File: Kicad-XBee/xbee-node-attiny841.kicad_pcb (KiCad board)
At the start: 2 copper layers, 58.5 x 56.8 mm, 21 parts, among them P1 Program, P2 XBee Adaptor, P3 CONN_5X2, P4 Battery, Q1 S1133, Q2 S9014, Q3 2N7000, U1 ATTINY4313-S, U2 MAX952ESA, U3 TPS77033

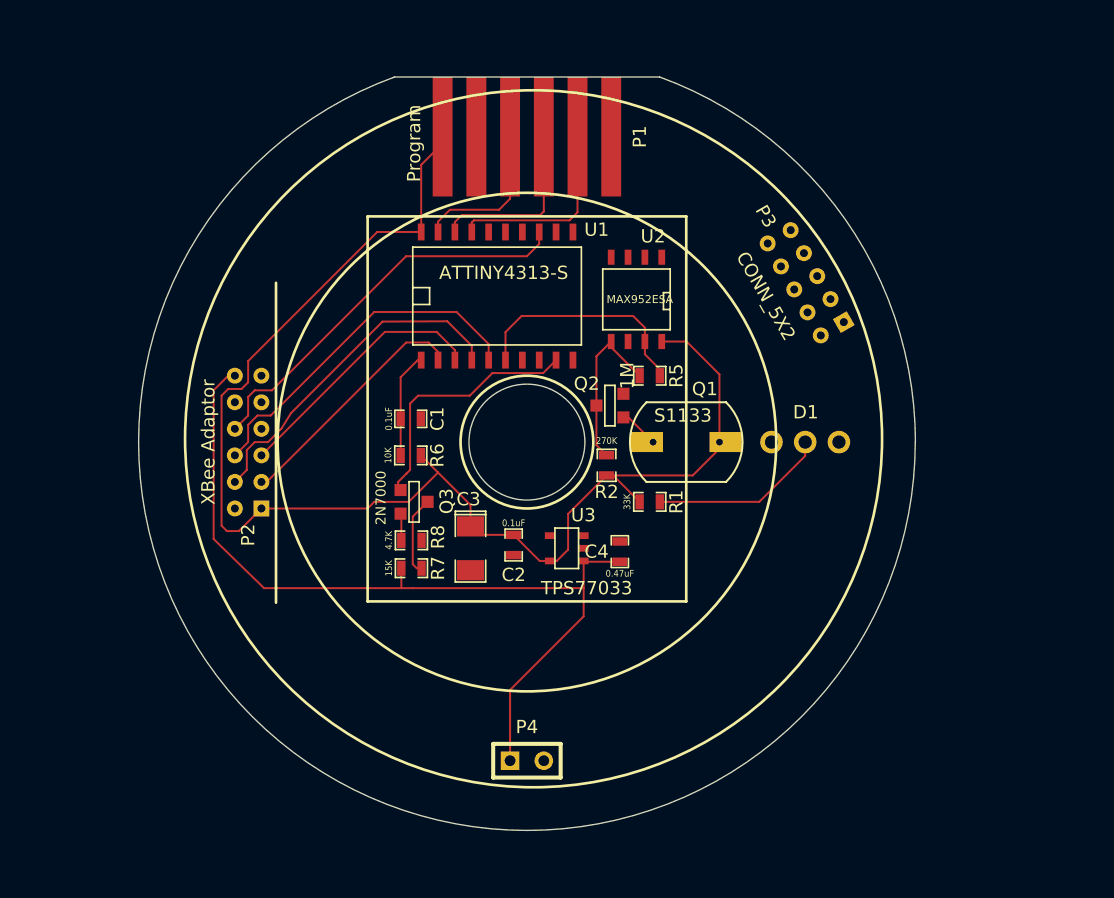
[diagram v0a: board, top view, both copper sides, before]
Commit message: Change to the ATTiny841 as the ATTiny4313 is 2.5mm high, and will interfere with the slotted disk. Completed layout but ground planes and power track widths still to be fixed.
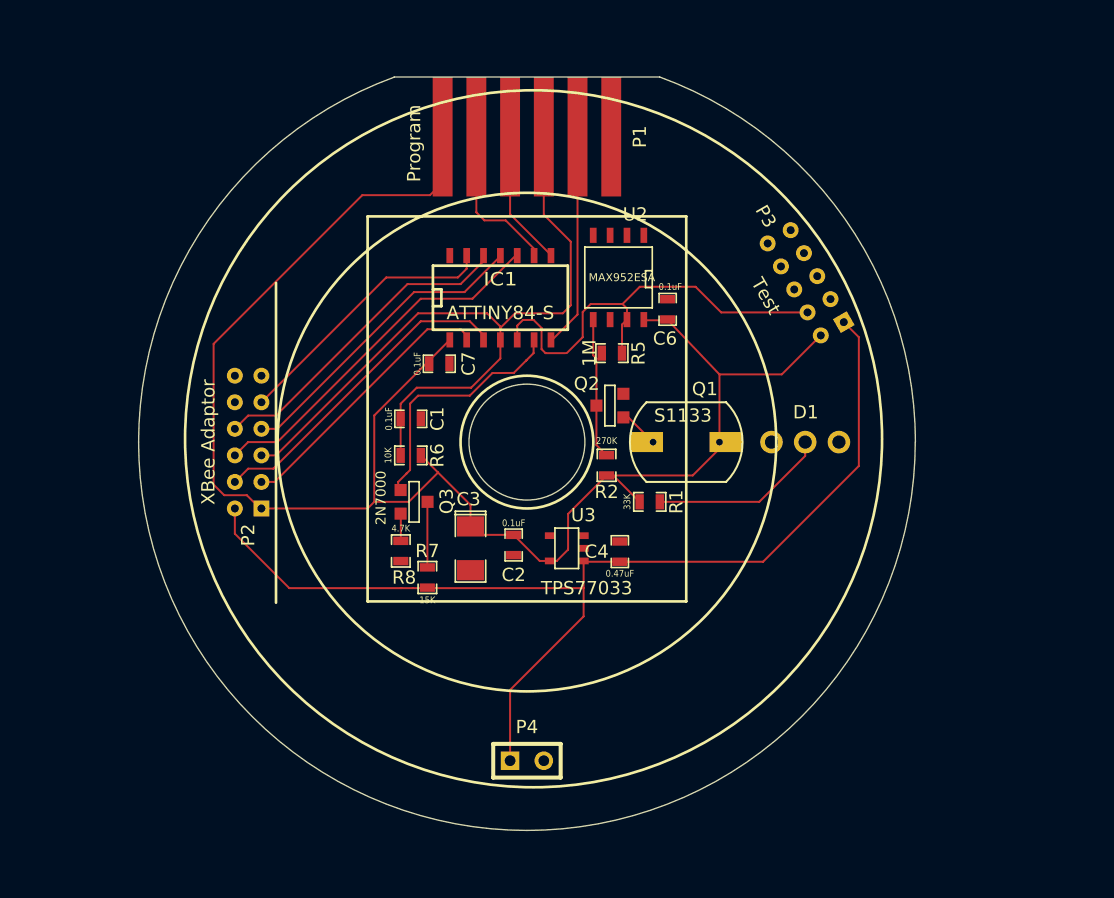
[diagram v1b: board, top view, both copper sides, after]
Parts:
- removed U1: ATTINY4313-S, SMD_Packages:SO20L
- added C6: 0.1uF, SMD_Packages:SM0603_Capa, F.Cu at (210.6, 90.0)
- added C7: 0.1uF, SMD_Packages:SM0603_Capa, F.Cu at (193.4, 94.1)
- added IC1: ATTINY84-S, SMD_Packages:SO14N, F.Cu at (198.0, 89.0)
- P3: value CONN_5X2 -> Test
- moved R5 3.32 mm to (206.4, 93.3)
- moved U2 2.13 mm to (206.9, 87.6)
- moved R7 1.39 mm to (192.5, 110.2), turned to 90 degrees
- moved R8 1.13 mm to (190.5, 108.2), turned to 270 degrees
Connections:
- P1 pad 2: Net-(P1-Pad2) -> /MOSI
- P1 pad 3: Net-(P1-Pad3) -> /Reset
- P1 pad 4: Net-(P1-Pad4) -> /MISO
- P1 pad 5: /Reset -> /SCK
- P2 pad 10: /Xbee-Reset -> Net-(P2-Pad10)
- P2 pad 12: /VBatt -> Net-(P2-Pad12)
- P2 pad 2: /Sleep-Rq -> /VBatt
- P2 pad 3: /Rx -> /Bootloader
- P2 pad 4: /CTS -> /Xbee-Reset
- P2 pad 5: /Tx -> /Reset
- P2 pad 6: /RTS -> /Sleep-Rq
- P2 pad 7: /Bootloader -> /Rx
- P2 pad 8: /On/Sleep -> /Tx
- P2 pad 9: /Reset -> /On/Sleep
- P3 pad 1: /Rx -> /VBatt
- P3 pad 10: /VBatt -> GND
- P3 pad 2: /Sleep-Rq -> VDD
- P3 pad 3: /Tx -> Net-(P3-Pad3)
- P3 pad 4: Net-(P3-Pad4) -> Net-(IC1-Pad5)
- P3 pad 6: /On/Sleep -> Net-(P3-Pad6)
- P3 pad 7: /Reset -> Net-(P3-Pad7)
- P3 pad 8: /Xbee-Reset -> Net-(P3-Pad8)
- P3 pad 9: GND -> Net-(P3-Pad9)
- R5 pad 2: Net-(P3-Pad5) -> Net-(IC1-Pad5)
- U2 pad 7: Net-(P3-Pad5) -> Net-(IC1-Pad5)
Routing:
- net /Reset: track 7.97 -> 57.6 mm
- net Net-(IC1-Pad5): track 0.00 -> 33.1 mm
- net /Sleep-Rq: track 0.00 -> 27.5 mm
- net /RTS: track 26.6 -> 0.00 mm
- net /CTS: track 25.7 -> 0.00 mm
- net /Xbee-Reset: track 0.00 -> 24.5 mm
- net VDD: track 102.6 -> 126.7 mm
- net /Bootloader: track 0.00 -> 21.2 mm
- net /VBatt: track 64.2 -> 82.3 mm
- net Net-(P3-Pad5): track 17.6 -> 0.00 mm
- net /MOSI: track 0.00 -> 16.2 mm
- net Net-(P1-Pad2): track 14.2 -> 0.00 mm
- net Net-(P1-Pad3): track 12.9 -> 0.00 mm
- net /SCK: track 0.00 -> 11.7 mm
- net Net-(P1-Pad4): track 11.6 -> 0.00 mm
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
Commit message: Complete board except for ground plane stitches.
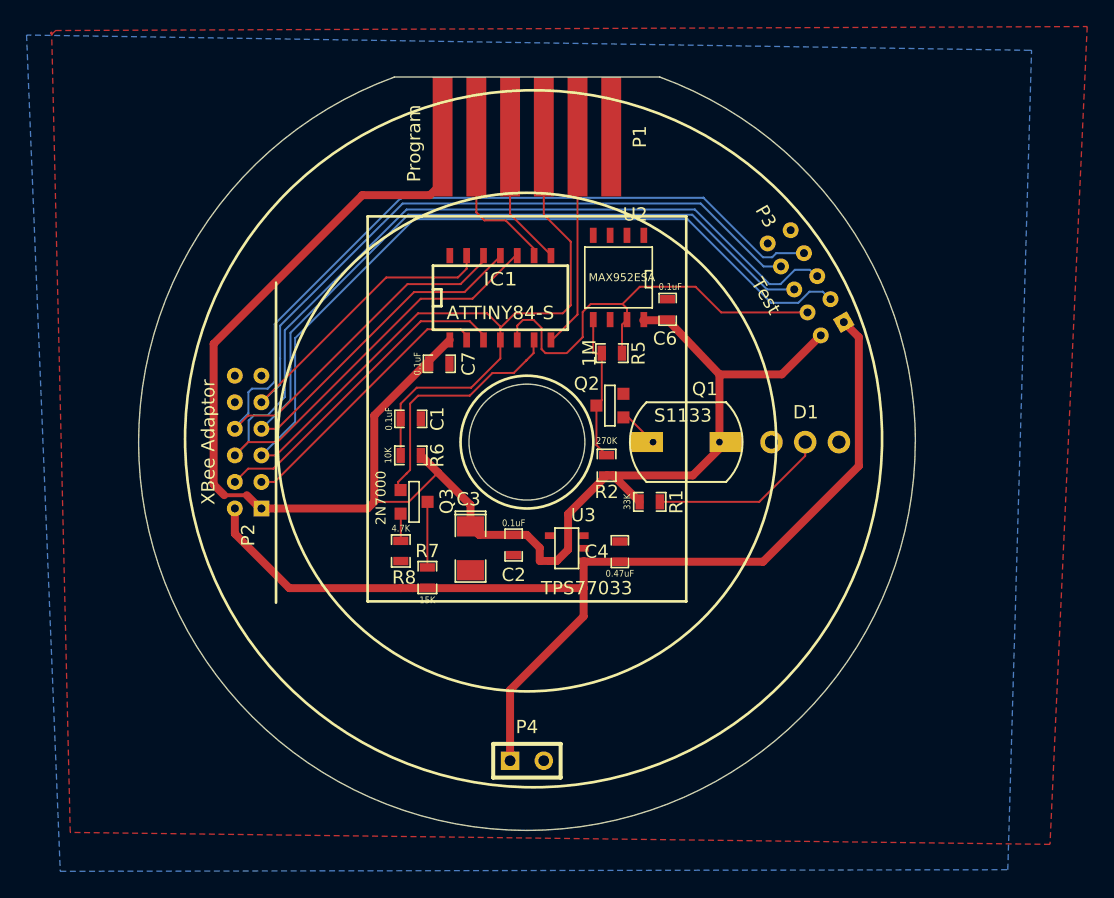
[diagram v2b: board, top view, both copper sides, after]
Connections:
- P3 pad 3: Net-(P3-Pad3) -> /Reset
- P3 pad 5: Net-(P3-Pad5) -> /Sleep-Rq
- P3 pad 6: Net-(P3-Pad6) -> /Rx
- P3 pad 7: Net-(P3-Pad7) -> /Tx
- P3 pad 8: Net-(P3-Pad8) -> /On/Sleep
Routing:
- net /Sleep-Rq: track 27.5 -> 85.9 mm
- net /Reset: track 57.6 -> 114.7 mm
- net /Tx: track 24.4 -> 80.2 mm
- net /Rx: track 23.4 -> 75.6 mm
- net /On/Sleep: track 20.6 -> 71.0 mm
- net Net-(Q2-Pad3): track 10.6 -> 11.3 mm
- net VDD: track 126.7 -> 127.3 mm
- added copper zone on B.Cu, net GND
- added copper zone on F.Cu, net GND

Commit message: Complete Kicad PCB
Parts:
- added Ref**: Val**, PhotoDiode:THROUGHVIA, F.Cu at (185.4, 101.8)
- added Ref**: Val**, PhotoDiode:THROUGHVIA, F.Cu at (200.6, 88.4)
- added Ref**: Val**, PhotoDiode:THROUGHVIA, F.Cu at (194.2, 98.7)
- added Ref**: Val**, PhotoDiode:THROUGHVIA, F.Cu at (193.8, 108.0)
- added Ref**: Val**, PhotoDiode:THROUGHVIA, F.Cu at (185.4, 107.9)
- added Ref**: Val**, PhotoDiode:THROUGHVIA, F.Cu at (195.7, 94.1)
- added Ref**: Val**, PhotoDiode:THROUGHVIA, F.Cu at (216.2, 92.5)
- added Ref**: Val**, PhotoDiode:THROUGHVIA, F.Cu at (210.1, 95.0)
- added Ref**: Val**, PhotoDiode:THROUGHVIA, F.Cu at (203.1, 94.7)
- moved P2 1.50 mm to (177.5, 100.0)
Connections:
- net Net-(IC1-Pad5) renamed /Count
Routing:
- net /Sleep-Rq: track 85.9 -> 89.0 mm
- net /Reset: track 114.7 -> 117.8 mm
- net /On/Sleep: track 71.0 -> 74.0 mm
- net /Rx: track 75.6 -> 78.6 mm
- net /Tx: track 80.2 -> 83.0 mm
- net VDD: track 127.3 -> 129.4 mm
- net /Xbee-Reset: track 24.5 -> 26.0 mm
- net /Bootloader: track 21.2 -> 22.7 mm
- net /VBatt: track 82.3 -> 83.5 mm

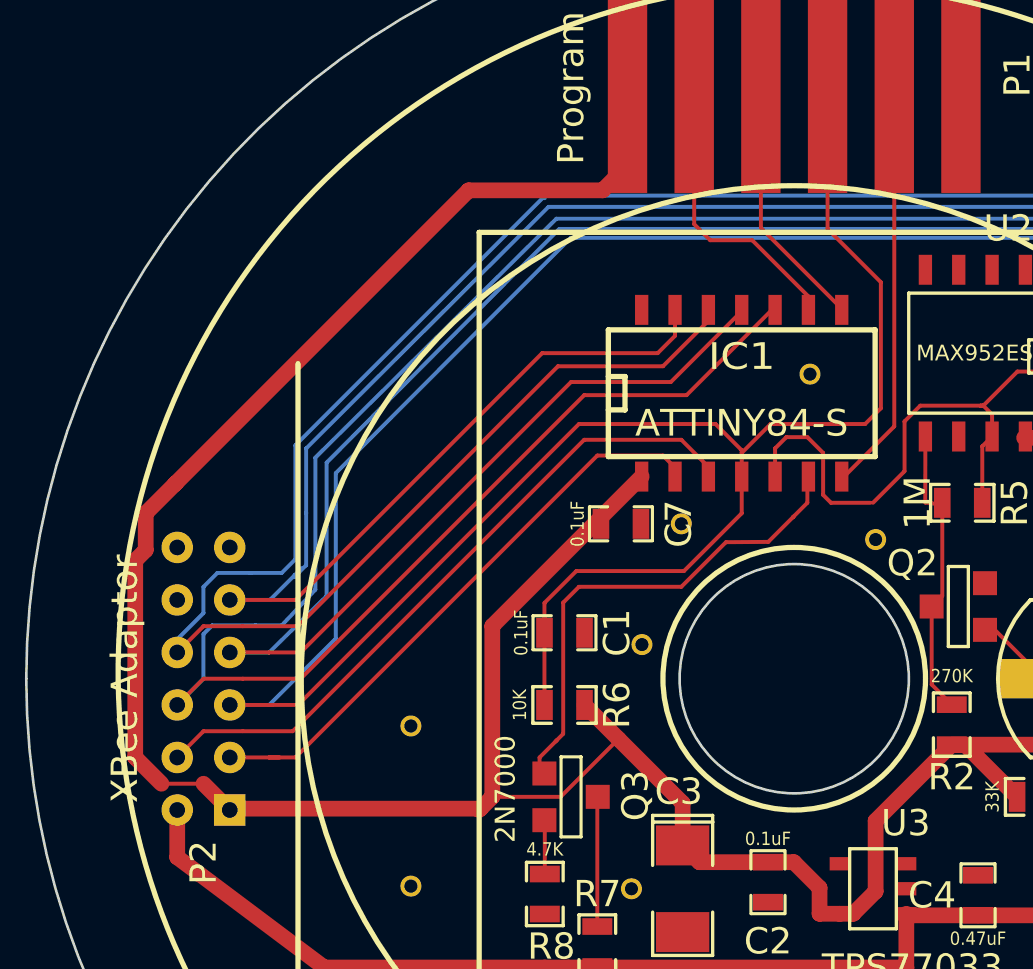
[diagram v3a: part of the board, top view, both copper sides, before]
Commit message: Modify PCB to interchange pins on AVR. The ATTiny841 has INT0 on pin 5 rather than pin 3 of the ATTiny84
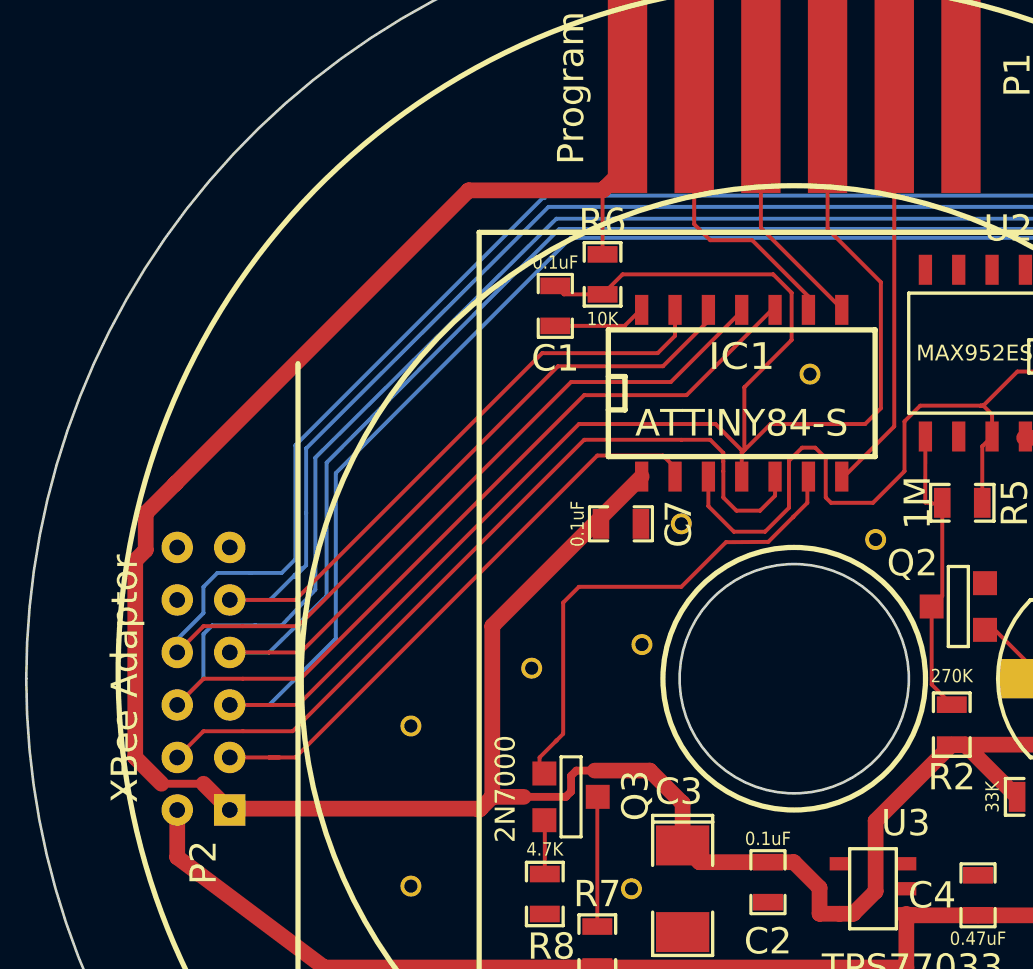
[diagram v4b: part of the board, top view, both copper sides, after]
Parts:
- added Ref**: Val**, Photodiode:THROUGHVIA, F.Cu at (190.0, 99.6)
- moved R6 16.5 mm to (192.7, 84.6), turned to 90 degrees
- moved C1 12.5 mm to (190.9, 85.8), turned to 270 degrees
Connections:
- IC1 pad 3: /Xbee-Reset -> /Count
- IC1 pad 5: /Count -> /Xbee-Reset
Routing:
- net /Count: track 33.1 -> 38.1 mm
- net /Xbee-Reset: track 26.0 -> 30.9 mm
- net GND: track 0.00 -> 3.54 mm
- net /Reset: track 117.8 -> 120.1 mm

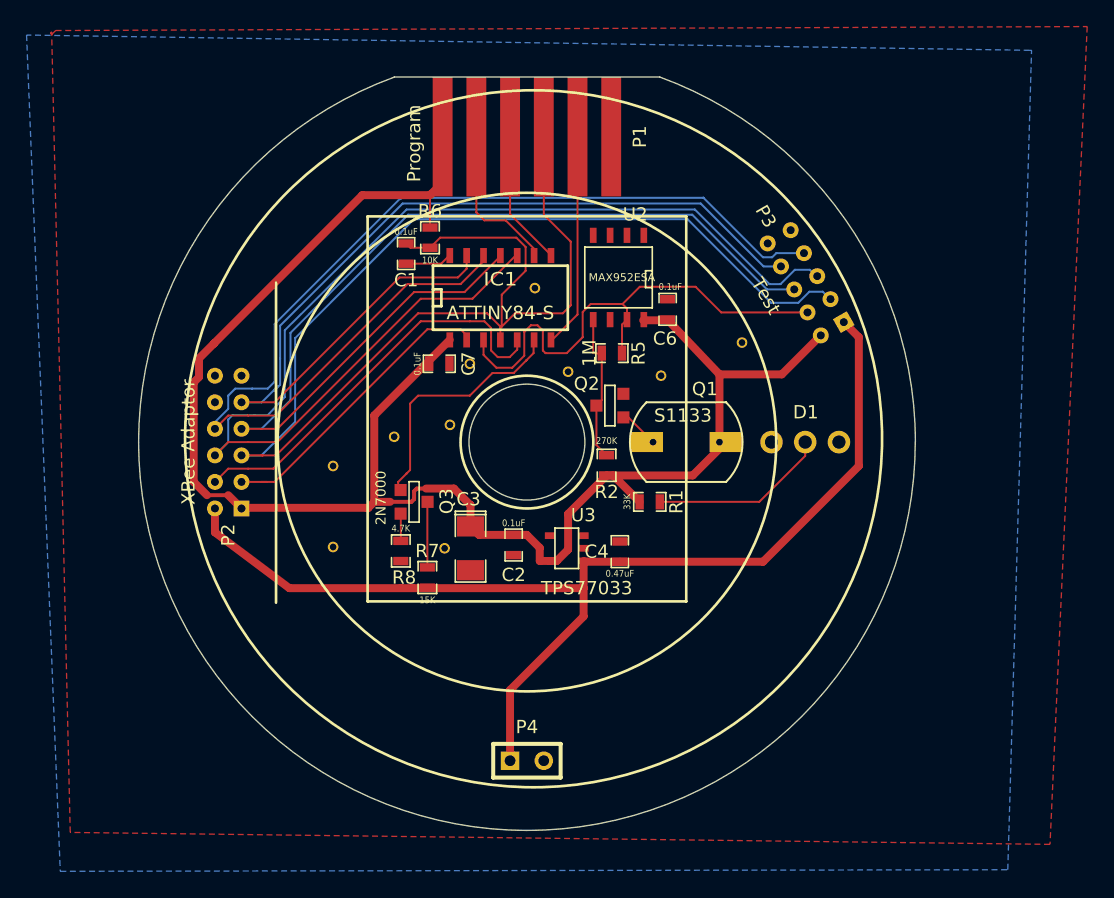
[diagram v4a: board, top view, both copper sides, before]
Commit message: Complete PCB adding additional pads for battery holders, removing edge connector and adding extra connectors to make a linear 12 pin XBee adapter.
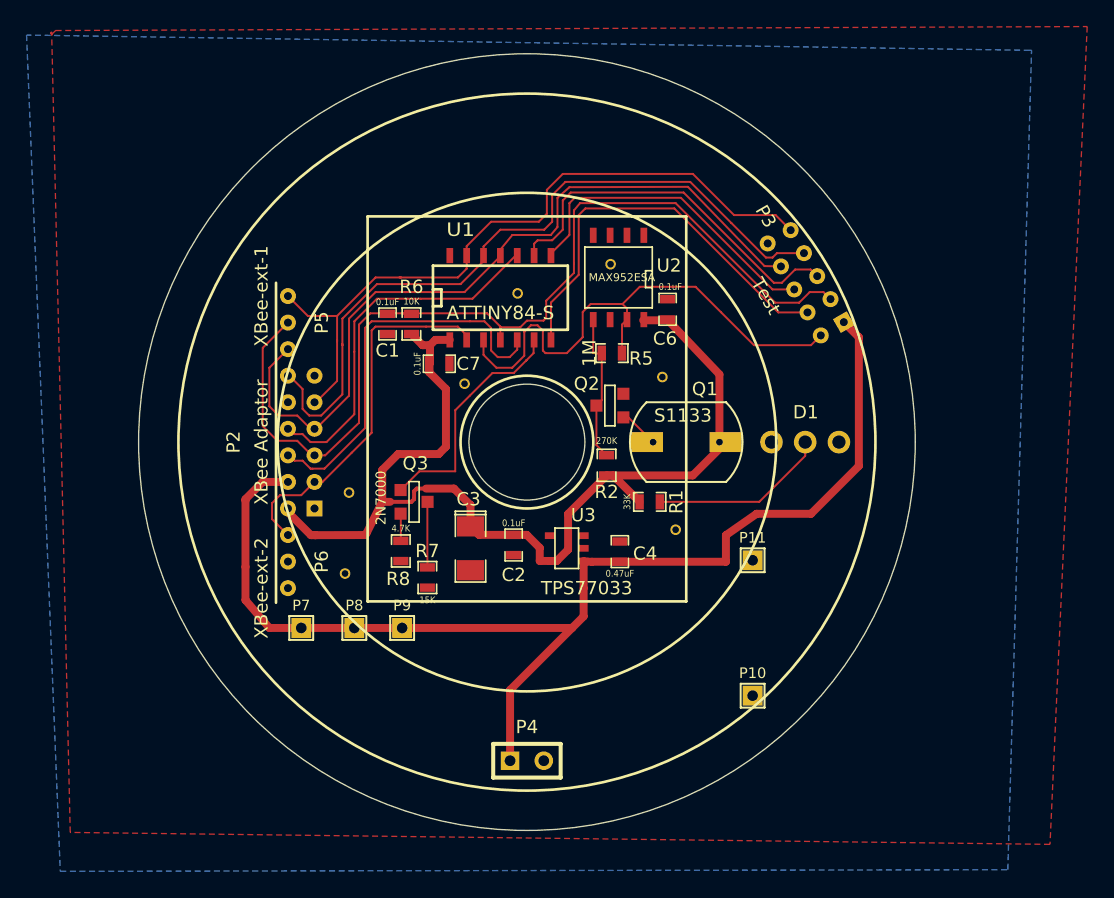
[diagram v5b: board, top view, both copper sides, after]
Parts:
- removed IC1: ATTINY84-S, SMD_Packages:SO14N
- removed P1: Program, PhotoDiode:edge_conn_6_pin
- removed Ref** (x9): Val**, PhotoDiode:THROUGHVIA
- removed Ref**: Val**, Photodiode:THROUGHVIA
- added P10: CONN_1, Connect:SIL-1, F.Cu at (217.0, 119.1)
- added P11: CONN_1, Connect:SIL-1, F.Cu at (217.0, 108.9)
- added P12: CONN_1, Photodiode:THROUGHVIA, F.Cu at (186.6, 103.8)
- added P13: CONN_1, Photodiode:THROUGHVIA, F.Cu at (199.3, 88.8)
- added P14: CONN_1, Photodiode:THROUGHVIA, F.Cu at (210.2, 95.1)
- added P15: CONN_1, Photodiode:THROUGHVIA, F.Cu at (195.3, 95.6)
- added P16: CONN_1, Photodiode:THROUGHVIA, F.Cu at (211.2, 106.6)
- added P17: CONN_1, Photodiode:THROUGHVIA, F.Cu at (186.3, 109.9)
- added P18: CONN_1, Photodiode:THROUGHVIA, F.Cu at (206.3, 86.6)
- added P5: XBee-ext-1, Photodiode:pin_header_2mm_1x3, F.Cu at (182.0, 91.0)
- added P6: XBee-ext-2, Photodiode:pin_header_2mm_1x3, F.Cu at (182.0, 109.0)
- added P7: CONN_1, Connect:SIL-1, F.Cu at (183.0, 114.0)
- added P8: CONN_1, Connect:SIL-1, F.Cu at (187.0, 114.0)
- added P9: CONN_1, Connect:SIL-1, F.Cu at (190.6, 114.0)
- added U1: ATTINY84-S, SMD_Packages:SOIC-14_N, F.Cu at (198.0, 89.0)
- moved R6 6.65 mm to (191.3, 91.1), turned to 270 degrees
- moved P2 5.50 mm to (183.0, 100.0)
- moved C1 5.48 mm to (189.5, 91.1)
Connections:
- P2 pad 1: VDD -> Net-(P2-Pad1)
- P2 pad 12: Net-(P2-Pad12) -> /Tx
- P2 pad 2: /VBatt -> VDD
- P2 pad 4: /Xbee-Reset -> /VBatt
- P2 pad 6: /Sleep-Rq -> /Xbee-Reset
- P2 pad 8: /Tx -> /Sleep-Rq
- P3 pad 2: VDD -> /Count
- P3 pad 4: /Count -> /MOSI
- P3 pad 5: /Sleep-Rq -> /SCK
- P3 pad 6: /Rx -> /MISO
- P3 pad 8: /On/Sleep -> /Rx
- P3 pad 9: Net-(P3-Pad9) -> /On/Sleep
- Q3 pad G: Net-(IC1-Pad6) -> /PowerControl
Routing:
- net /Sleep-Rq: track 89.0 -> 27.5 mm
- net VDD: track 129.7 -> 80.7 mm
- net /Reset: track 120.1 -> 73.6 mm
- net /Tx: track 83.0 -> 55.9 mm
- net /On/Sleep: track 74.0 -> 54.1 mm
- net /Rx: track 78.6 -> 59.4 mm
- net Net-(IC1-Pad6): track 18.9 -> 0.00 mm
- net /PowerControl: track 0.00 -> 18.1 mm
- net /SCK: track 11.7 -> 28.6 mm
- net /MOSI: track 16.2 -> 31.0 mm
- net /MISO: track 10.2 -> 24.5 mm
- net /VBatt: track 83.5 -> 90.6 mm
- net /Bootloader: track 22.7 -> 28.2 mm
- net GND: track 3.54 -> 0.04 mm
- net /Count: track 38.1 -> 40.5 mm
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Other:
- board size 58.5 x 56.8 mm -> 58.5 x 58.5 mm
